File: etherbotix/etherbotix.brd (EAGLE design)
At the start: 100 x 50 mm, 28 parts, among them J1 J3011G21DNL, J2 22-03-5035, J3 22-03-5035, J4 22-03-5045, J5 22-03-5045, J6 1760520000, J7 1760490000, J8 502443-0470, J9 502443-0470, U1 STM32F407V, U2 TLK110, U3 OKI-78SR-5/1.5-W36-C, U4 TLV1117-33IKVURG3KVU, U5 ACS711ELCTR-25AB-T, U6 ACS711ELCTR-25AB-T, U7 MAX481CSA, U8 74LS126D, X1 25MHZ

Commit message: routed, still needs cleanup
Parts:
- added ACT: BLUE, fergs:LED0603
- added C1, C2: 2.2uF, fergs:C0603
- added C10, C14, C15, C16, C23, C24, C25, C26, C3, C36, C37, C38, C5, C6, C7, C8, C9: 0.1uF, fergs:C0603
- added C11, C27, C28, C31: 4.7uF, fergs:0603
- added C12, C19, C20, C21, C22: 1uF, fergs:C0603
- added C13, C17, C18, C39, C4, C40: 100pF, fergs:C0603
- added C29, C30, C32: 1000PF, fergs:0603
- added C33, C34, C35: 10uF, fergs:C0603
- added C41: 56uF, fergs:OSCON_SVPF_6.3MM
- added ERR: RED, fergs:LED0603
- added PWR: GREEN, fergs:LED0603
- added R10, R11, R12, R13, R5, R6, R7, R9: 10k, fergs:0603
- added R14, R15, R16, R17: 49R9, fergs:0603
- added R18, R21, R23, R29: 2K2, fergs:0603
- added R19, R20, R24, R25, R26, R28, R8: 1k, fergs:0603
- added R22: 4K87, fergs:0603
- added R27: 15k, fergs:0603
- added R30: 120, fergs:0603
- added R31, R32: 750, fergs:0603
- added X2: (no value), ethernet:OSCILLATOR
- U3: value OKI-78SR-5/1.5-W36-C -> OKI-78SR-5
- U4: value TLV1117-33IKVURG3KVU -> TLV1117
- moved IMU 27.2 mm to (78.4, 15.2), turned to 0 degrees
- moved U2 17.5 mm to (59.7, 40.3)
- moved X1 13.6 mm to (70.5, 20.3), turned to 180 degrees
- moved U7 13.2 mm to (26.4, 31.4), turned to 180 degrees
- moved J1 12.7 mm to (96.5, 30.5)
- moved U8 11.3 mm to (34.9, 24.8), turned to 270 degrees
- moved J5 10.2 mm to (12.7, 38.1), turned to 180 degrees
- moved J4 10.2 mm to (12.7, 32.7), turned to 180 degrees
- moved U6 9.13 mm to (24.6, 19.7)
- moved R2 7.67 mm to (34.9, 41.3), turned to 180 degrees
- moved J2 7.65 mm to (12.7, 27.3), turned to 180 degrees
- moved J3 7.65 mm to (12.7, 22.2), turned to 180 degrees
- moved R1 7.43 mm to (34.9, 43.2)
- moved R4 7.24 mm to (90.8, 42.5), turned to 180 degrees
- moved R3 6.33 mm to (90.8, 44.1), turned to 180 degrees
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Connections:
- removed net A3: U$1.P$4, U1.18
- removed net ETH_REF_CLK: U1.24
- removed net MCO: U1.67, U2.34
- removed net USBDM: U1.70
- removed net USBDP: U1.71
- new net +12V-AUX: J7.2, MOTORS.VIN1, MOTORS.VIN2, R27.2, U5.3, U5.4
- new net ACT: ACT.A, U1.9
- new net D3: U$1.P$4, U1.47
- new net ERR: ERR.A, U1.8
- new net ETH_CLK: U1.24, U2.34, X2.3
- new net N$15: C40.1, U1.12, X1.3
- new net N$16: J1.3, R14.2, U2.17
- new net N$17: R18.2, U2.20
- new net N$18: J1.2, U2.27
- new net N$19: J1.7, R16.2, U2.14
- new net N$20: J1.11, U2.26
- new net N$21: J1.8, R17.1, U2.13
- new net N$22: J1.1, R20.1
- new net N$23: J1.12, R19.1
- new net N$24: C33.1, C36.1, C37.1, C38.1, U2.18, U2.23, U2.37
- new net N$25: R21.1, U2.21
- new net N$26: R22.2, U2.24
- new net N$27: R23.1, U2.39
- new net N$28: PWR.C, R26.2
- new net N$30: ERR.C, R25.2
- new net N$31: ACT.C, R24.2
- new net PHY_RST: U1.38, U2.29
- new net V_SENSE: R27.1, R28.2, U1.15
- net +12V: now also C41.+; no longer MOTORS.VIN1, MOTORS.VIN2
- net +5V: now also C14.1, C34.1, R10.2, R11.2, R12.2, R13.2, R5.2, R6.2, R7.2
- net A1: now also U1.17; no longer U1.36
- net A2: now also U1.18; no longer U1.17
- net AUX_CURRENT_SENSE: now also U1.36
- net D4: now also U1.79; no longer U1.47
- net D5: now also U1.54; no longer U1.79
- net ETH_MDIO: now also R29.1
- net GND: now also C1.2, C10.2, C11.2, C12.2, C13.2, C14.2, C15.2, C16.2, C17.2, C18.2, C19.2, C2.2, C20.2, C21.2, C22.2, C23.2, C24.2, C25.2, C26.2, C27.2, C28.2, C29.2, C3.2, C30.2, C31.2, C32.2, C33.2, C34.2, C35.2, C36.2, C37.2, C38.2, C39.2, C4.2, C40.2, C41.-, C5.2, C6.2, C7.2, C8.2, C9.2, J1.10, J1.9, J1.A, J1.B, R22.1, R24.1, R25.1, R26.1, R28.1, R32.1, U1.20, X1.2, X1.4, X2.2
- net M1_EN: now also U1.44
- net M1_ENC_A: now also C13.1, U1.59; no longer U1.31
- net M1_ENC_B: now also C4.1, U1.60
- net M2_EN: now also U1.65
- net M2_ENC_A: now also C18.1, U1.31; no longer U1.59
- net M2_ENC_B: now also C17.1, U1.91; no longer U1.60
- net N$1: now also J1.4, R15.1, U2.16; no longer J7.2, U5.3, U5.4
- net N$10: now also R30.1, R31.1
- net N$11: now also R30.2, R32.2
- net N$12: now also R7.1, R8.1
- net N$13: now also R6.1
- net N$14: now also R8.2
- net N$3: now also C39.1, U1.13, X1.1; no longer U1.100, U1.11, U1.19, U1.28, U1.50, U1.75
- net N$4: now also C1.1
- net N$5: now also C2.1
- net N$6: now also R10.1
- net N$7: now also R11.1
- net N$8: now also R13.1
- net N$9: now also R12.1
- net SERVO_CURRENT_SENSE: now also U1.23
- net USART1_RX: now also R9.1
- net USART2_RX: now also R5.1
- net VCC: now also C10.1, C11.1, C12.1, C15.1, C16.1, C19.1, C20.1, C21.1, C22.1, C23.1, C24.1, C25.1, C26.1, C27.1, C28.1, C29.1, C3.1, C30.1, C31.1, C32.1, C35.1, C5.1, C6.1, C7.1, C8.1, C9.1, J1.5, J1.6, PWR.A, R14.1, R15.2, R16.1, R17.2, R18.1, R19.2, R20.2, R21.2, R23.2, R29.2, R31.2, R9.2, U1.100, U1.11, U1.19, U1.21, U1.22, U1.28, U1.50, U1.75, U2.22, U2.32, U2.48, X2.1, X2.4
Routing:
- net VCC: track 0.00 -> 357.9 mm, vias 0 -> 14
- net +5V: track 0.00 -> 241.2 mm, vias 0 -> 7
- net GND: track 0.00 -> 207.2 mm, vias 0 -> 30
- net M1_SENSE: track 0.00 -> 102.9 mm, vias 0 -> 6
- net M2_A: track 0.00 -> 85.4 mm, vias 0 -> 3
- net D7: track 0.00 -> 77.6 mm, vias 0 -> 2
- net D6: track 0.00 -> 76.4 mm, vias 0 -> 2
- net M2_ENC_B: track 0.00 -> 72.5 mm, vias 0 -> 4
- net D4: track 0.00 -> 64.8 mm, vias 0 -> 2
- net A1: track 0.00 -> 64.1 mm, vias 0 -> 4
- net A2: track 0.00 -> 63.4 mm, vias 0 -> 4
- net +12V-AUX: track 0.00 -> 59.9 mm
- net AUX_CURRENT_SENSE: track 0.00 -> 57.9 mm, vias 0 -> 2
- net M2_ENC_A: track 0.00 -> 57.2 mm, vias 0 -> 2
- net A0: track 0.00 -> 55.6 mm, vias 0 -> 4
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- added copper zone on layer 1, net +12V
- added copper zone on layer 1, net +12V-AUX
- added copper zone on layer 1, net +5V
- added copper zone on layer 1, net GND
- added copper zone on layer 16, net GND
- added copper zone on layer 1, net VCC
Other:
- board text added: "A0"
- board text added: "A1"
- board text added: "A2"
- board text added: "D3"
- board text added: "D4"
- board text added: "D5"
- board text added: "D6"
- board text added: "D7"
- board text removed: "LARGE CAP"
- board text removed: "SHORT CAPS"

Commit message: pass DRC
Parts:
- moved U4 0.63 mm to (34.6, 8.57)
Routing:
- net VCC: track 357.9 -> 360.4 mm, vias 14 -> 12
- net AUX_CURRENT_SENSE: track 57.9 -> 59.0 mm
- net +5V: track 241.2 -> 241.7 mm
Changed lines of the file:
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@@
 <attribute name="VOLTAGE" value="5" x="16.51" y="13.97" size="1.778" layer="27" display="off"/>
 </element>
-<element name="U4" library="power" package="DPAK" value="TLV1117" x="34.6075" y="9.2075" rot="R90"/>
+<element name="U4" library="power" package="DPAK" value="TLV1117" x="34.6075" y="8.5725" rot="R90"/>
 <element name="U5" library="allegro" package="SOIC8" value="ACS711ELCTR-25AB-T" x="26.67" y="7.62" smashed="yes" rot="R270">
 <attribute name="CURRENT" value="25A" x="26.67" y="7.62" size="1.778" layer="27" rot="R270" display="off"/>
@@
 <wire x1="37.225" y1="13.575" x2="36.83" y2="13.97" width="0.4064" layer="1"/>
 <wire x1="36.83" y1="13.97" x2="36.83" y2="16.32" width="0.4064" layer="1"/>
-<wire x1="36.83" y1="16.32" x2="36.8975" y2="16.3875" width="0.4064" layer="1"/>
+<wire x1="36.83" y1="16.32" x2="36.8975" y2="15.7525" width="0.4064" layer="1"/>
 <wire x1="28.4725" y1="3.4925" x2="28.4725" y2="5.5" width="0.254" layer="1"/>
 <wire x1="28.4725" y1="5.5" x2="28.2575" y2="5.715" width="0.254" layer="1"/>
@@
 <wire x1="18.0975" y1="48.895" x2="18.0975" y2="42.085" width="0.254" layer="1"/>
 <wire x1="18.0975" y1="42.085" x2="18.05" y2="42.0375" width="0.254" layer="1"/>
-<wire x1="32.3175" y1="16.3875" x2="28.41625" y2="15.875" width="0.6096" layer="1"/>
+<wire x1="32.3175" y1="15.7525" x2="28.41625" y2="15.875" width="0.6096" layer="1"/>
 <wire x1="28.41625" y1="15.875" x2="27.58625" y2="16.705" width="0.6096" layer="1"/>
 <wire x1="27.58625" y1="16.705" x2="27.58625" y2="18.2925" width="0.6096" layer="1"/>
@@
 <wire x1="32.54375" y1="19.52625" x2="32.22625" y2="19.20875" width="0.254" layer="1"/>
 <wire x1="32.22625" y1="19.20875" x2="32.22625" y2="16.47875" width="0.254" layer="1"/>
-<wire x1="32.22625" y1="16.47875" x2="32.3175" y2="16.3875" width="0.254" layer="1"/>
+<wire x1="32.22625" y1="16.47875" x2="32.3175" y2="15.7525" width="0.254" layer="1"/>
 </signal>
 <signal name="VCC">
@@
 <contactref element="C15" pad="1"/>
 <wire x1="29.27" y1="9.525" x2="34.925" y2="9.525" width="0.254" layer="1"/>
-<wire x1="34.925" y1="9.525" x2="34.6075" y2="9.2075" width="0.254" layer="1"/>
+<wire x1="34.925" y1="9.525" x2="34.6075" y2="8.5725" width="0.254" layer="1"/>
 <wire x1="29.7675" y1="11.1125" x2="32.7025" y2="11.1125" width="0.4064" layer="1"/>
-<wire x1="32.7025" y1="11.1125" x2="34.6075" y2="9.2075" width="0.4064" layer="1"/>
+<wire x1="32.7025" y1="11.1125" x2="34.6075" y2="8.5725" width="0.4064" layer="1"/>
 <wire x1="28.2575" y1="28.3591" x2="28.2575" y2="29.5275" width="0.254" layer="1"/>
 <wire x1="28.2575" y1="29.5275" x2="28.8925" y2="30.1625" width="0.254" layer="1"/>
@@
 <contactref element="R29" pad="2"/>
 <contactref element="R31" pad="2"/>
-<wire x1="30.0475" y1="2.425" x2="31.75" y2="4.1275" width="0.254" layer="1"/>
-<via x="31.75" y="4.1275" extent="1-16" drill="0.4064"/>
-<wire x1="31.75" y1="4.1275" x2="33.655" y2="6.0325" width="0.254" layer="16"/>
-<wire x1="33.655" y1="6.0325" x2="37.30625" y2="6.0325" width="0.254" layer="16"/>
-<wire x1="37.30625" y1="6.0325" x2="39.21125" y2="7.9375" width="0.254" layer="16"/>
-<via x="39.21125" y="7.9375" extent="1-16" drill="0.4064"/>
-<wire x1="39.21125" y1="7.9375" x2="39.37" y2="8.09625" width="0.254" layer="1"/>
-<wire x1="39.37" y1="8.09625" x2="39.37" y2="10.63625" width="0.254" layer="1"/>
+<wire x1="30.0475" y1="2.425" x2="32.0675" y2="4.445" width="0.254" layer="1"/>
+<wire x1="32.0675" y1="4.445" x2="38.1" y2="4.445" width="0.254" layer="1"/>
+<wire x1="38.1" y1="4.445" x2="39.37" y2="5.715" width="0.254" layer="1"/>
+<wire x1="39.37" y1="5.715" x2="39.37" y2="10.63625" width="0.254" layer="1"/>
 <wire x1="39.0525" y1="11.58875" x2="39.0525" y2="11.43" width="0.254" layer="1"/>
 <wire x1="39.0525" y1="11.43" x2="39.21125" y2="11.58875" width="0.254" layer="1"/>
@@
 <wire x1="29.27" y1="8.255" x2="30.7975" y2="8.255" width="0.254" layer="1"/>
 <wire x1="30.7975" y1="8.255" x2="31.115" y2="7.9375" width="0.254" layer="1"/>
-<wire x1="31.115" y1="7.9375" x2="31.115" y2="5.715" width="0.254" layer="1"/>
-<wire x1="31.115" y1="5.715" x2="31.4325" y2="5.3975" width="0.254" layer="1"/>
-<wire x1="31.4325" y1="5.3975" x2="37.465" y2="5.3975" width="0.254" layer="1"/>
-<wire x1="37.465" y1="5.3975" x2="38.25875" y2="6.19125" width="0.254" layer="1"/>
+<wire x1="31.115" y1="7.9375" x2="31.115" y2="5.23875" width="0.254" layer="1"/>
+<wire x1="31.115" y1="5.23875" x2="31.4325" y2="4.92125" width="0.254" layer="1"/>
+<wire x1="31.4325" y1="4.92125" x2="37.7825" y2="4.92125" width="0.254" layer="1"/>
+<wire x1="37.7825" y1="4.92125" x2="38.25875" y2="5.3975" width="0.254" layer="1"/>
 <wire x1="56.245" y1="28.32" x2="56.245" y2="29.32125" width="0.254" layer="1"/>
 <wire x1="56.245" y1="29.32125" x2="55.08625" y2="30.48" width="0.254" layer="1"/>
@@
 <wire x1="37.7825" y1="22.225" x2="38.25875" y2="21.74875" width="0.254" layer="16"/>
 <wire x1="38.25875" y1="21.74875" x2="38.25875" y2="10.4775" width="0.254" layer="16"/>
-<wire x1="38.25875" y1="10.4775" x2="38.25875" y2="6.19125" width="0.254" layer="1"/>
+<wire x1="38.25875" y1="10.4775" x2="38.25875" y2="5.3975" width="0.254" layer="1"/>
 <via x="38.25875" y="10.4775" extent="1-16" drill="0.4064"/>
 </signal>
@@
 <contactref element="U1" pad="41"/>
 <contactref element="U1" pad="44"/>
-<wire x1="33.02" y1="2.54" x2="35.2425" y2="4.7625" width="0.254" layer="1"/>
-<wire x1="35.2425" y1="4.7625" x2="39.84625" y2="4.7625" width="0.254" layer="1"/>
+<wire x1="33.02" y1="2.54" x2="34.44875" y2="3.96875" width="0.254" layer="1"/>
+<wire x1="34.44875" y1="3.96875" x2="38.4175" y2="3.96875" width="0.254" layer="1"/>
 <wire x1="53.745" y1="28.32" x2="53.745" y2="29.28125" width="0.254" layer="1"/>
 <wire x1="53.745" y1="29.28125" x2="53.6575" y2="29.36875" width="0.254" layer="1"/>
@@
 <wire x1="41.75125" y1="17.78" x2="41.75125" y2="10.95375" width="0.254" layer="1"/>
 <wire x1="41.75125" y1="10.95375" x2="42.545" y2="10.16" width="0.254" layer="1"/>
-<wire x1="42.545" y1="10.16" x2="42.545" y2="7.46125" width="0.254" layer="1"/>
-<wire x1="39.84625" y1="4.7625" x2="42.545" y2="7.46125" width="0.254" layer="1"/>
+<wire x1="42.545" y1="10.16" x2="42.545" y2="8.09625" width="0.254" layer="1"/>
+<wire x1="38.4175" y1="3.96875" x2="42.545" y2="8.09625" width="0.254" layer="1"/>
 </signal>
 <signal name="M1_A">
 <contactref element="MOTORS" pad="1A"/>
 <contactref element="U1" pad="39"/>
-<wire x1="35.56" y1="2.54" x2="37.1475" y2="4.1275" width="0.254" layer="1"/>
-<wire x1="37.1475" y1="4.1275" x2="40.005" y2="4.1275" width="0.254" layer="1"/>
-<wire x1="40.005" y1="4.1275" x2="43.02125" y2="7.14375" width="0.254" layer="1"/>
+<wire x1="35.56" y1="2.54" x2="36.5125" y2="3.4925" width="0.254" layer="1"/>
+<wire x1="36.5125" y1="3.4925" x2="38.735" y2="3.4925" width="0.254" layer="1"/>
+<wire x1="38.735" y1="3.4925" x2="43.02125" y2="7.77875" width="0.254" layer="1"/>
 <wire x1="54.745" y1="28.32" x2="54.745" y2="26.32875" width="0.254" layer="1"/>
 <wire x1="54.745" y1="26.32875" x2="54.61" y2="26.19375" width="0.254" layer="1"/>
@@
 <wire x1="42.2275" y1="18.0975" x2="42.2275" y2="11.43" width="0.254" layer="1"/>
 <wire x1="42.2275" y1="11.43" x2="43.02125" y2="10.63625" width="0.254" layer="1"/>
-<wire x1="43.02125" y1="10.63625" x2="43.02125" y2="7.14375" width="0.254" layer="1"/>
+<wire x1="43.02125" y1="10.63625" x2="43.02125" y2="7.77875" width="0.254" layer="1"/>
 </signal>
 <signal name="M1_B">
 <contactref element="MOTORS" pad="1B"/>
 <contactref element="U1" pad="42"/>
-<wire x1="38.1" y1="2.54" x2="39.21125" y2="2.54" width="0.254" layer="1"/>
-<wire x1="39.21125" y1="2.54" x2="43.4975" y2="6.82625" width="0.254" layer="1"/>
-<wire x1="43.4975" y1="6.82625" x2="43.4975" y2="10.95375" width="0.254" layer="1"/>
+<wire x1="38.1" y1="2.54" x2="38.57625" y2="2.54" width="0.254" layer="1"/>
+<wire x1="38.57625" y1="2.54" x2="43.4975" y2="7.46125" width="0.254" layer="1"/>
+<wire x1="43.4975" y1="7.46125" x2="43.4975" y2="10.95375" width="0.254" layer="1"/>
 <wire x1="53.245" y1="28.32" x2="53.245" y2="27.21" width="0.254" layer="1"/>
 <wire x1="53.245" y1="27.21" x2="53.0225" y2="26.9875" width="0.254" layer="1"/>

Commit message: fix part number of 1760510000
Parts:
- J6: value 1760520000 -> 1760510000
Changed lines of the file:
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@@
 <element name="J4" library="molex" package="5267-4" value="22-03-5045" x="12.7" y="32.7025" rot="R180"/>
 <element name="J5" library="molex" package="5267-4" value="22-03-5045" x="12.7" y="38.1" rot="R180"/>
-<element name="J6" library="headers" package="1760490000" value="1760520000" x="5.08" y="13.0175" smashed="yes" rot="R270">
+<element name="J6" library="headers" package="1760490000" value="1760510000" x="5.08" y="13.0175" smashed="yes" rot="R270">
 <attribute name="NAME" x="8.89" y="14.9225" size="1.27" layer="21" rot="R180"/>
 </element>

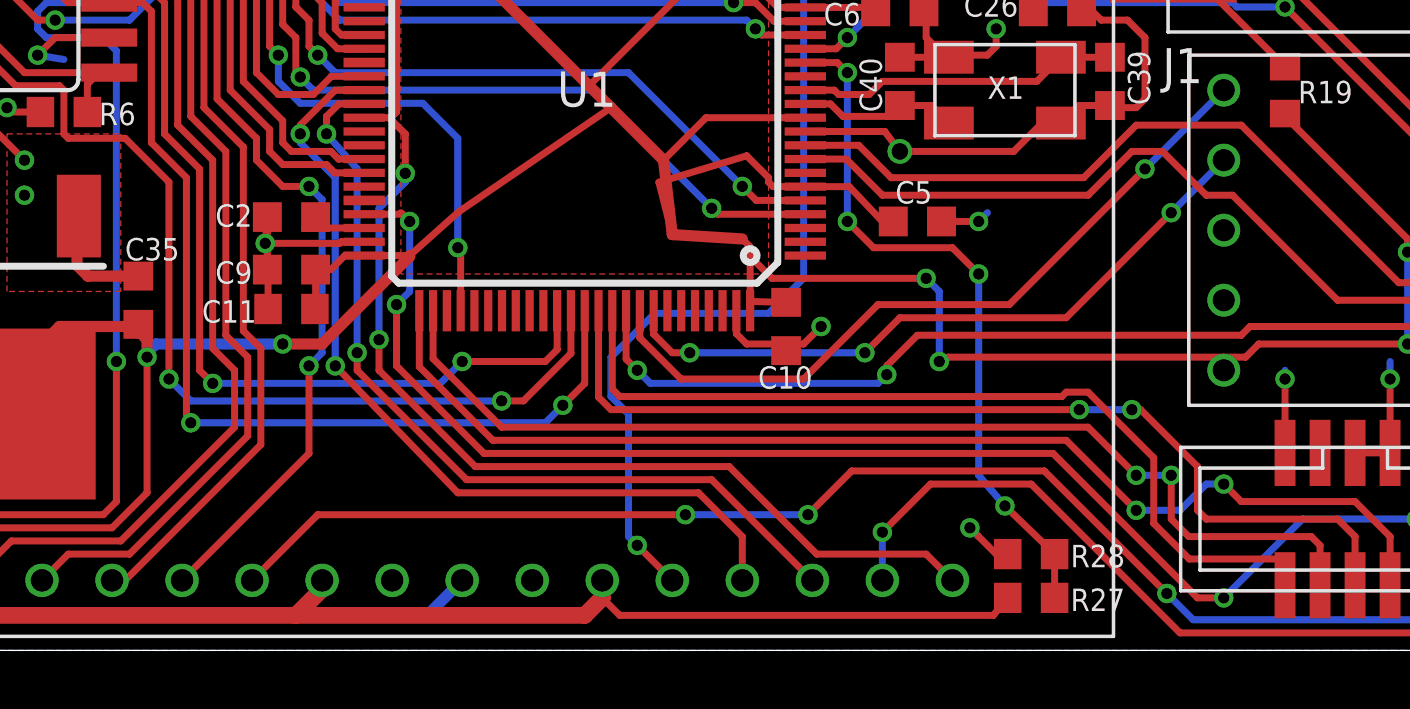
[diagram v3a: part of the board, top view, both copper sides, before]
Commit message: add testpads
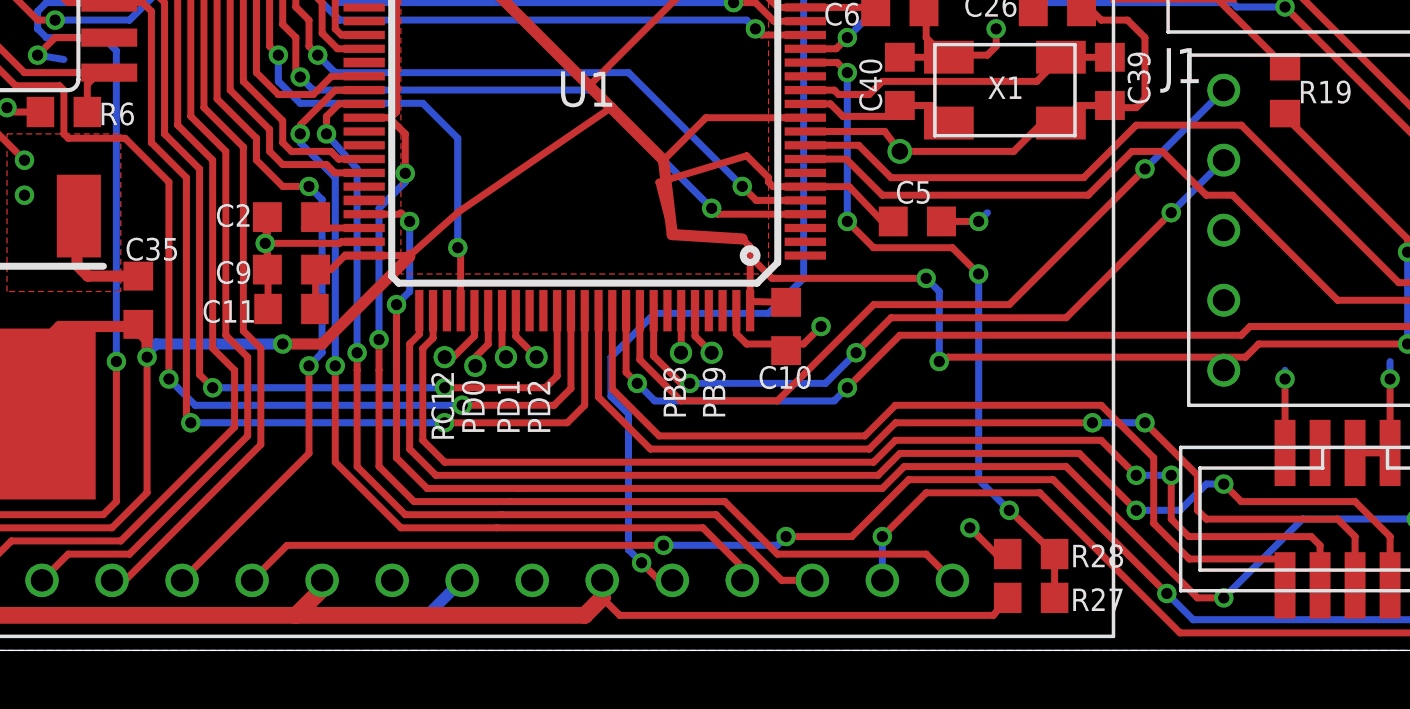
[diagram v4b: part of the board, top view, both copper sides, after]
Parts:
- added T1, T2, T3, T4, T5, T6: TESTPAD, fergs:TEST
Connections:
- new net PB8: T2.T, U1.95
- new net PB9: T1.T, U1.96
- new net PC12: T3.T, U1.80
- new net PD0: T4.T, U1.81
- new net PD1: T5.T, U1.82
- new net PD2: T6.T, U1.83
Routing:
- net TDI: track 39.1 -> 42.0 mm
- net TCK: track 42.3 -> 45.2 mm
- net TMS: track 51.8 -> 54.4 mm
- net PC12: track 0.00 -> 2.32 mm
- net PD0: track 0.00 -> 2.20 mm
- net M2_B: track 30.8 -> 32.9 mm
- net M2_EN: track 41.8 -> 43.9 mm
- net PD2: track 0.00 -> 2.00 mm
- net PB9: track 0.00 -> 1.78 mm
- net PD1: track 0.00 -> 1.74 mm
- net PB8: track 0.00 -> 1.53 mm
- net I2C1_SDA: track 24.7 -> 26.1 mm
- net M2_PWM: track 31.1 -> 32.4 mm
- net I2C1_SCL: track 27.1 -> 28.2 mm
- net USART2_RX: track 37.8 -> 38.6 mm
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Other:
- board text added: "PB8"
- board text added: "PB9"
- board text added: "PC12"
- board text added: "PD0"
- board text added: "PD1"
- board text added: "PD2"
